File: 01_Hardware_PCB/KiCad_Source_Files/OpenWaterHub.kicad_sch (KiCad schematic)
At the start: 183 parts, among them J1 DWIN, J10 MOTOR3, J11 MOTOR4, J12 USB type B, J2 ON/OFF, J3 MOTOR1, J4 PWR 24V, J5 S1, J6 S2, J7 MOTOR2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

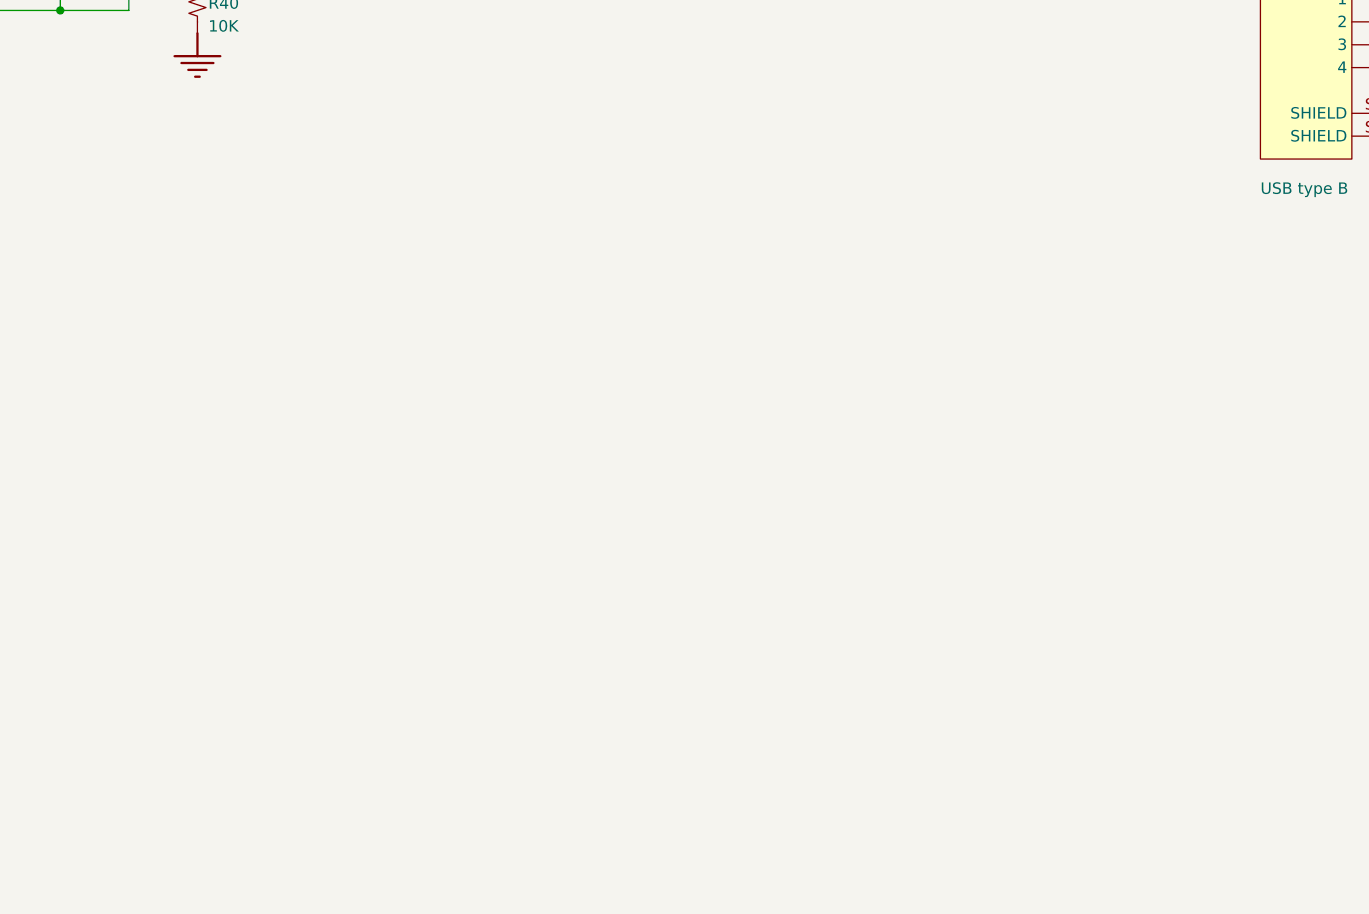
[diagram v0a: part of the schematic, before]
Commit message: Updated Schematic Text Guides
Co-Authored-By: Ahmed I. Ahmed, M.Sc. <dev.ahmed.ibrahim@gmail.com>
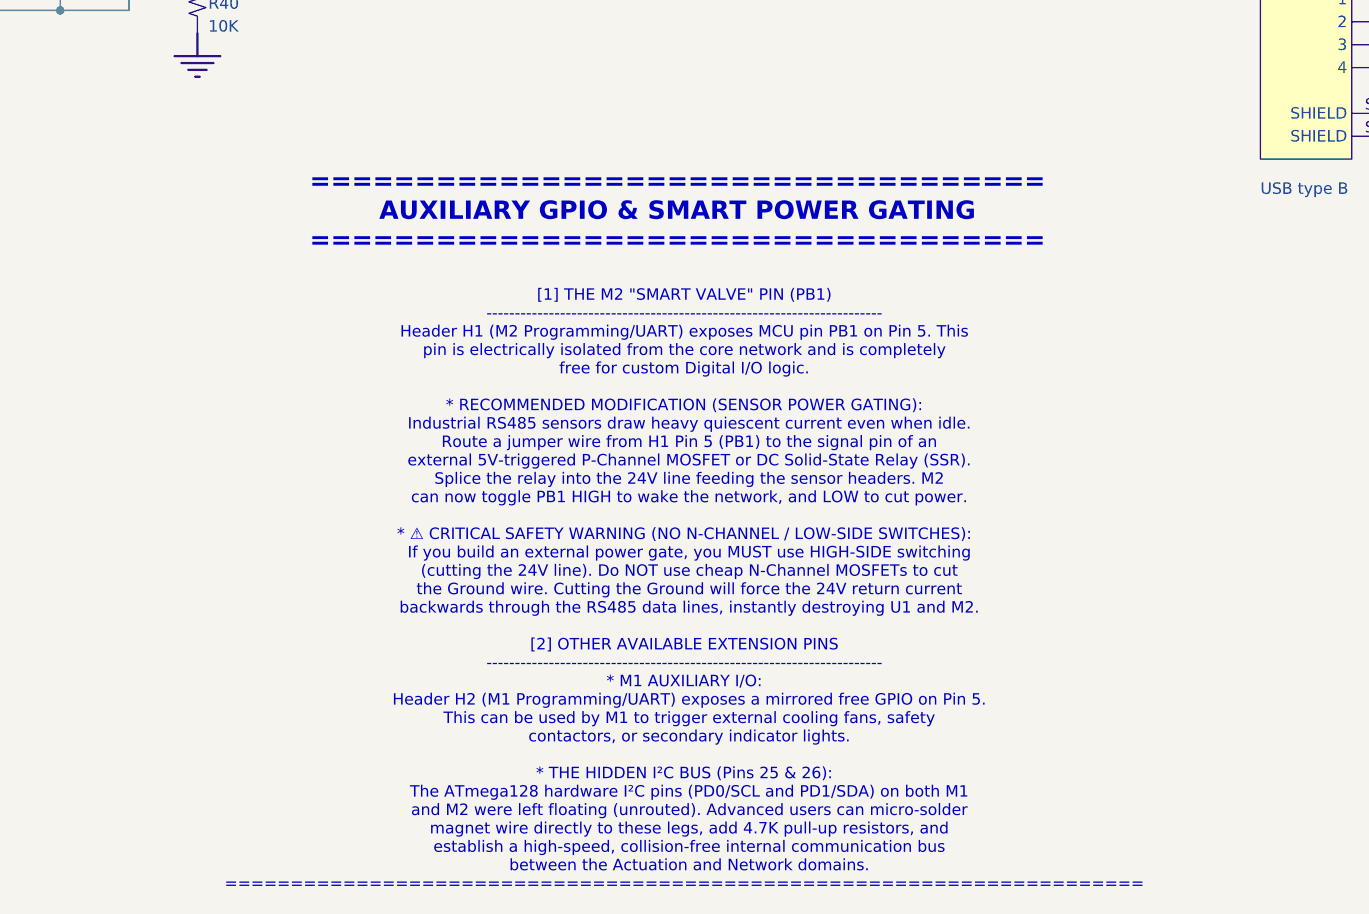
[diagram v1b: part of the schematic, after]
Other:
- note added: "=================================== AUXILIARY GPIO & SMART POWER GATING ==================================="
- note added: "[1] THE M2 "SMART VALVE" PIN (PB1) ---------------------------------------------------------------------- Header H1 (M2 Programming/UART) exposes MCU pin PB1 on Pin 5. This pin is electrically isolated from the core network and is completely free for custom Digital I/O logic. * RECOMMENDED MODIFICATION (SENSOR POWER GATING): Industrial RS485 sensors draw heavy quiescent current even when idle. Ro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"
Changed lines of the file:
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@@
+		)
+	)
+	(text "\n===================================\nAUXILIARY GPIO & SMART POWER GATING\n==================================="
+		(exclude_from_sim no)
+		(at 514.35 301.498 0)
+		(effects
+			(font
+				(size 2.032 2.032)
+				(thickness 0.4064)
+				(bold yes)
+			)
 		)
 	)
@@
 			)
 		)
+	)
+	(text "\n[1] THE M2 \"SMART VALVE\" PIN (PB1)\n----------------------------------------------------------------------\nHeader H1 (M2 Programming/UART) exposes MCU pin PB1 on Pin 5. This \npin is electrically isolated from the core network and is completely \nfree for custom Digital I/O logic.\n\n* RECOMMENDED MODIFICATION (SENSOR POWER GATING): \n  Industrial RS485 sensors draw heavy quiescent current even when idle. \n  Route a jumper wire from H1 Pin 5 (PB1) to the signal pin of an \n  external 5V-triggered P-Channel MOSFET or DC Solid-State Relay (SSR). \n  Splice the relay into the 24V line feeding the sensor headers. M2 \n  can now toggle PB1 HIGH to wake the network, and LOW to cut power.\n\n* ⚠️ CRITICAL SAFETY WARNING (NO N-CHANNEL / LOW-SIDE SWITCHES): \n  If you build an external power gate, you MUST use HIGH-SIDE switching \n  (cutting the 24V line). Do NOT use cheap N-Channel MOSFETs to cut \n  the Ground wire. Cutting the Ground will force the 24V return current \n  backwards through the RS485 data lines, instantly destroying U1 and M2.\n\n[2] OTHER AVAILABLE EXTENSION PINS\n----------------------------------------------------------------------\n* M1 AUXILIARY I/O: \n  Header H2 (M1 Programming/UART) exposes a mirrored free GPIO on Pin 5. \n  This can be used by M1 to trigger external cooling fans, safety \n  contactors, or secondary indicator lights.\n\n* THE HIDDEN I²C BUS (Pins 25 & 26): \n  The ATmega128 hardware I²C pins (PD0/SCL and PD1/SDA) on both M1 \n  and M2 were left floating (unrouted). Advanced users can micro-solder \n  magnet wire directly to these legs, add 4.7K pull-up resistors, and \n  establish a high-speed, collision-free internal communication bus \n  between the Actuation and Network domains.\n======================================================================"
+		(exclude_from_sim no)
+		(at 515.112 344.17 0)
+		(effects
+			(font
+				(size 1.27 1.27)
+			)
+		)

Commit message: Updated Schematic Text again
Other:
- note added: "[3] SENSOR NETWORKING (12V vs 24V RS485 SENSORS) ---------------------------------------------------------------------- The 4-pin RS485 sensor ports (J5, J6, J8, J9) and the DWIN port (J1) route the raw 'VIN' power net to Pin 4 to power external nodes. There is NO dedicated 12V regulator on this board. * If you supply 24V to the main input (J4), the sensors receive 24V. * If you want to use stric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"
- moved on the sheet: C11, C12, C22, C23, C24, C25, C27, C28, C33, C34, C35, C36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
